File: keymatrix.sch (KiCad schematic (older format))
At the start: 18 parts

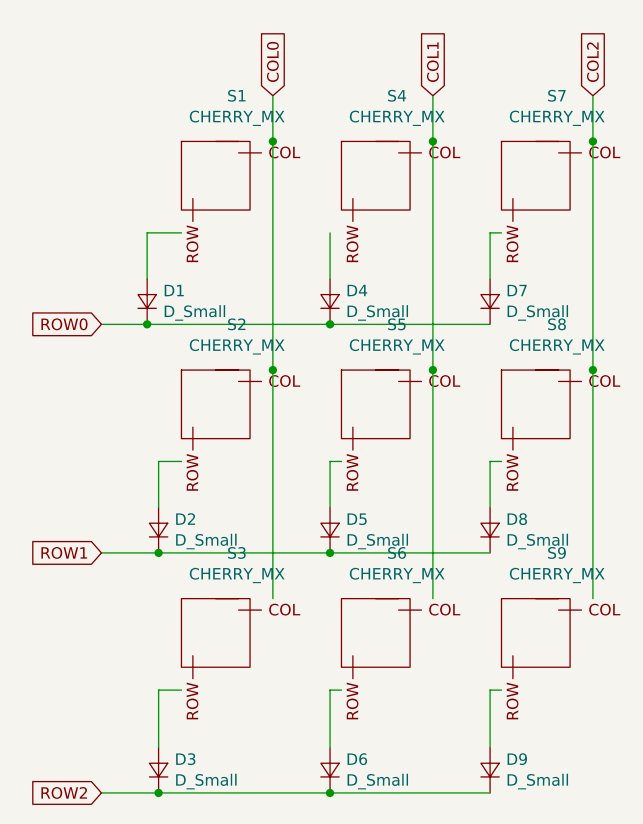
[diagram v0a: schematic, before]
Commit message: Move parts - part one
No traces yet, only part movement
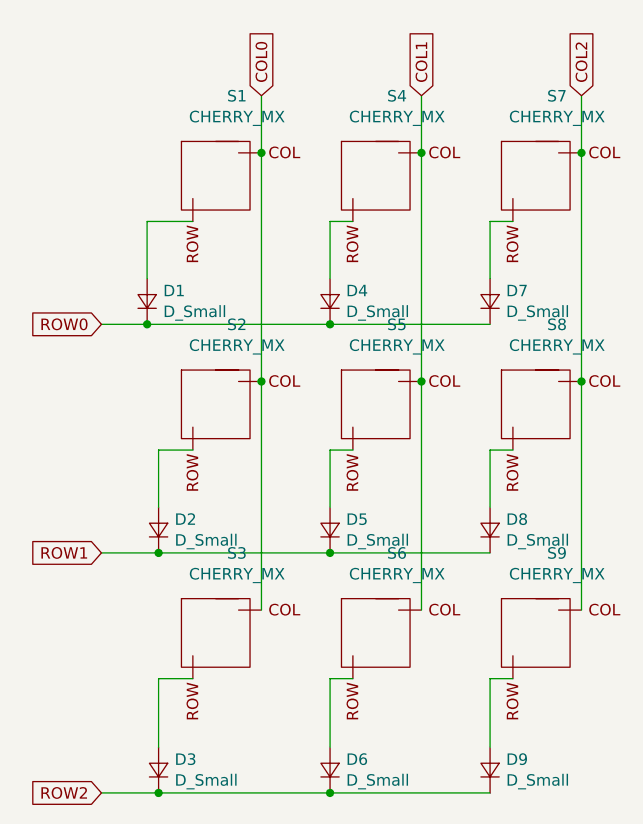
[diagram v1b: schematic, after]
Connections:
- wire segments 35 -> 36
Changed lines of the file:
@@
 $EndComp
 Wire Wire Line
-	1900 1000 1900 2000
-Connection ~ 1900 2000
+	1350 1350 1350 1600
 Wire Wire Line
-	1900 2000 1900 3000
+	2850 1600 2850 1350
 Wire Wire Line
-	2600 1000 2600 2000
-Connection ~ 2600 2000
+	2850 1350 2950 1350
 Wire Wire Line
-	2600 2000 2600 3000
+	1550 2350 1400 2350
 Wire Wire Line
-	3300 1000 3300 2000
-Connection ~ 3300 2000
+	1400 2350 1400 2600
 Wire Wire Line
-	3300 2000 3300 3000
+	2150 2600 2150 2350
 Wire Wire Line
-	1500 1400 1350 1400
+	2150 2350 2250 2350
 Wire Wire Line
-	1350 1400 1350 1600
+	2850 2600 2850 2350
 Wire Wire Line
-	2150 1400 2150 1600
+	2850 2350 2950 2350
 Wire Wire Line
-	2850 1600 2850 1400
+	2850 3650 2850 3350
 Wire Wire Line
-	2850 1400 2900 1400
+	2850 3350 2950 3350
 Wire Wire Line
-	1500 2400 1400 2400
+	2150 3650 2150 3350
 Wire Wire Line
-	1400 2400 1400 2600
+	2150 3350 2250 3350
 Wire Wire Line
-	2150 2600 2150 2400
+	1400 3650 1400 3350
 Wire Wire Line
-	2150 2400 2200 2400
-Wire Wire Line
-	2850 2600 2850 2400
-Wire Wire Line
-	2850 2400 2900 2400
-Wire Wire Line
-	2850 3650 2850 3400
-Wire Wire Line
-	2850 3400 2900 3400
-Wire Wire Line
-	2150 3650 2150 3400
-Wire Wire Line
-	2150 3400 2200 3400
-Wire Wire Line
-	1400 3650 1400 3400
-Wire Wire Line
-	1400 3400 1500 3400
+	1400 3350 1550 3350
 Wire Wire Line
 	2850 1800 2150 1800
@@
 Wire Wire Line
 	2150 3850 1400 3850
-Wire Wire Line
-	1900 1000 1900 800
-Connection ~ 1900 1000
-Wire Wire Line
-	2600 1000 2600 800
-Connection ~ 2600 1000
-Wire Wire Line
-	3300 1000 3300 800
-Connection ~ 3300 1000
 Text GLabel 1150 1800 0    50   Input ~ 0
 ROW0
@@
 Text GLabel 1150 3850 0    50   Input ~ 0
 ROW2
-Text GLabel 1900 800  1    50   Input ~ 0
+Text GLabel 1850 800  1    50   Input ~ 0
 COL0
-Text GLabel 2600 800  1    50   Input ~ 0
+Text GLabel 2550 800  1    50   Input ~ 0
 COL1
-Text GLabel 3300 800  1    50   Input ~ 0
+Text GLabel 3250 800  1    50   Input ~ 0
 COL2
+Wire Wire Line
+	3250 800  3250 1050
+Connection ~ 3250 1050
+Wire Wire Line
+	3250 1050 3250 2050
+Connection ~ 3250 2050
+Wire Wire Line
+	3250 2050 3250 3050
+Wire Wire Line
+	2150 1350 2250 1350
+Wire Wire Line
+	2150 1350 2150 1600
+Wire Wire Line
+	1350 1350 1550 1350
+Wire Wire Line
+	1850 800  1850 1050
+Wire Wire Line
+	2550 800  2550 1050
+Connection ~ 2550 1050
+Wire Wire Line
+	2550 1050 2550 2050
+Connection ~ 2550 2050
+Wire Wire Line
+	2550 2050 2550 3050
+Connection ~ 1850 1050
+Wire Wire Line
+	1850 1050 1850 2050
+Connection ~ 1850 2050
+Wire Wire Line
+	1850 2050 1850 3050
 $EndSCHEMATC

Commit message: Add some tracks - hate it
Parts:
- S1, S2, S3, S4, S5, S6, S7, S8, S9: symbol keyboard-stuff:CHERRY_MX -> k6-rescue:CHERRY_MX-keyboard-stuff
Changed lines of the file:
@@
 $EndDescr
 $Comp
-L keyboard-stuff:CHERRY_MX S1
+L k6-rescue:CHERRY_MX-keyboard-stuff S1
 U 1 1 5ECF56C1
 P 1650 1150
+AR Path="/5ECF56C1" Ref="S1"  Part="1"
+AR Path="/5EBEA505/5ECF56C1" Ref="S1"  Part="1"
 F 0 "S1" H 1743 1498 50  0000 C CNN
 F 1 "CHERRY_MX" H 1743 1407 50  0000 C CNN
@@
 $EndComp
 $Comp
-L keyboard-stuff:CHERRY_MX S4
+L k6-rescue:CHERRY_MX-keyboard-stuff S4
 U 1 1 5ECF5BA1
 P 2350 1150
+AR Path="/5ECF5BA1" Ref="S4"  Part="1"
+AR Path="/5EBEA505/5ECF5BA1" Ref="S4"  Part="1"
 F 0 "S4" H 2443 1498 50  0000 C CNN
 F 1 "CHERRY_MX" H 2443 1407 50  0000 C CNN
@@
 $EndComp
 $Comp
-L keyboard-stuff:CHERRY_MX S7
+L k6-rescue:CHERRY_MX-keyboard-stuff S7
 U 1 1 5ECF6210
 P 3050 1150
+AR Path="/5ECF6210" Ref="S7"  Part="1"
+AR Path="/5EBEA505/5ECF6210" Ref="S7"  Part="1"
 F 0 "S7" H 3143 1498 50  0000 C CNN
 F 1 "CHERRY_MX" H 3143 1407 50  0000 C CNN
@@
 $EndComp
 $Comp
-L keyboard-stuff:CHERRY_MX S2
+L k6-rescue:CHERRY_MX-keyboard-stuff S2
 U 1 1 5ECF6801
 P 1650 2150
+AR Path="/5ECF6801" Ref="S2"  Part="1"
+AR Path="/5EBEA505/5ECF6801" Ref="S2"  Part="1"
 F 0 "S2" H 1743 2498 50  0000 C CNN
 F 1 "CHERRY_MX" H 1743 2407 50  0000 C CNN
@@
 $EndComp
 $Comp
-L keyboard-stuff:CHERRY_MX S5
+L k6-rescue:CHERRY_MX-keyboard-stuff S5
 U 1 1 5ECF6E6B
 P 2350 2150
+AR Path="/5ECF6E6B" Ref="S5"  Part="1"
+AR Path="/5EBEA505/5ECF6E6B" Ref="S5"  Part="1"
 F 0 "S5" H 2443 2498 50  0000 C CNN
 F 1 "CHERRY_MX" H 2443 2407 50  0000 C CNN
@@
 $EndComp
 $Comp
-L keyboard-stuff:CHERRY_MX S8
+L k6-rescue:CHERRY_MX-keyboard-stuff S8
 U 1 1 5ECF7338
 P 3050 2150
+AR Path="/5ECF7338" Ref="S8"  Part="1"
+AR Path="/5EBEA505/5ECF7338" Ref="S8"  Part="1"
 F 0 "S8" H 3143 2498 50  0000 C CNN
 F 1 "CHERRY_MX" H 3143 2407 50  0000 C CNN
@@
 $EndComp
 $Comp
-L keyboard-stuff:CHERRY_MX S3
+L k6-rescue:CHERRY_MX-keyboard-stuff S3
 U 1 1 5ECF7BDC
 P 1650 3150
+AR Path="/5ECF7BDC" Ref="S3"  Part="1"
+AR Path="/5EBEA505/5ECF7BDC" Ref="S3"  Part="1"
 F 0 "S3" H 1743 3498 50  0000 C CNN
 F 1 "CHERRY_MX" H 1743 3407 50  0000 C CNN
@@
 $EndComp
 $Comp
-L keyboard-stuff:CHERRY_MX S6
+L k6-rescue:CHERRY_MX-keyboard-stuff S6
 U 1 1 5ECF83E9
 P 2350 3150
+AR Path="/5ECF83E9" Ref="S6"  Part="1"
+AR Path="/5EBEA505/5ECF83E9" Ref="S6"  Part="1"
 F 0 "S6" H 2443 3498 50  0000 C CNN
 F 1 "CHERRY_MX" H 2443 3407 50  0000 C CNN
@@
 $EndComp
 $Comp
-L keyboard-stuff:CHERRY_MX S9
+L k6-rescue:CHERRY_MX-keyboard-stuff S9
 U 1 1 5ECF8C8A
 P 3050 3150
+AR Path="/5ECF8C8A" Ref="S9"  Part="1"
+AR Path="/5EBEA505/5ECF8C8A" Ref="S9"  Part="1"
 F 0 "S9" H 3143 3498 50  0000 C CNN
 F 1 "CHERRY_MX" H 3143 3407 50  0000 C CNN
